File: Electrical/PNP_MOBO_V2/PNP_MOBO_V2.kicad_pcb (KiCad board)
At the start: 4 copper layers, 0 parts

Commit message: wip pcbv2
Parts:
- added A10: Pololu_Breakout_DRV8825, Module:Pololu_Breakout-16_15.2x20.3mm, F.Cu at (122.8, 87.6)
- added A5: Pololu_Breakout_DRV8825, Module:Pololu_Breakout-16_15.2x20.3mm, F.Cu at (70.7, 87.6)
- added A6: Pololu_Breakout_DRV8825, Module:Pololu_Breakout-16_15.2x20.3mm, F.Cu at (96.7, 61.6)
- added A7: Pololu_Breakout_DRV8825, Module:Pololu_Breakout-16_15.2x20.3mm, F.Cu at (96.7, 87.6)
- added A8: Pololu_Breakout_DRV8825, Module:Pololu_Breakout-16_15.2x20.3mm, F.Cu at (122.7, 61.6)
- added A9: Pololu_Breakout_DRV8825, Module:Pololu_Breakout-16_15.2x20.3mm, F.Cu at (70.8, 61.6)
- added C1: 0.1uf, Capacitor_SMD:C_0603_1608Metric_Pad1.08x0.95mm_HandSolder, F.Cu at (-17.8, 2.99)
- added C12: 10uf, Capacitor_SMD:C_0603_1608Metric_Pad1.08x0.95mm_HandSolder, F.Cu at (-13.5, 2.99)
- added C13: 0.1uf, Capacitor_SMD:C_0603_1608Metric_Pad1.08x0.95mm_HandSolder, F.Cu at (-13.5, 5.50)
- added C16: 10uf, Capacitor_SMD:C_0603_1608Metric_Pad1.08x0.95mm_HandSolder, F.Cu at (-13.5, 8.01)
- added C17: 0.1uf, Capacitor_SMD:C_0603_1608Metric_Pad1.08x0.95mm_HandSolder, F.Cu at (-13.5, 10.5)
- added C2: 10uf, Capacitor_SMD:C_0603_1608Metric_Pad1.08x0.95mm_HandSolder, F.Cu at (-17.8, 5.50)
- added C20: 100uF, Capacitor_SMD:CP_Elec_8x10, F.Cu at (160.0, 72.6)
- added C21: 0.1uF, Capacitor_SMD:C_0603_1608Metric_Pad1.08x0.95mm_HandSolder, F.Cu at (-13.5, 13.0)
- added C22: 0.1uF, Capacitor_SMD:C_0603_1608Metric_Pad1.08x0.95mm_HandSolder, F.Cu at (149.3, 110.5)
- added C23: 100uF, Capacitor_SMD:CP_Elec_8x10, F.Cu at (88.0, 94.3)
- added C24: 0.1uF, Capacitor_SMD:C_0603_1608Metric_Pad1.08x0.95mm_HandSolder, F.Cu at (149.3, 113.0)
- added C25: 100uF, Capacitor_SMD:CP_Elec_8x10, F.Cu at (114.6, 68.3)
- added C26: 0.1uF, Capacitor_SMD:C_0603_1608Metric_Pad1.08x0.95mm_HandSolder, F.Cu at (149.3, 115.5)
- added C27: 100uF, Capacitor_SMD:CP_Elec_8x10, F.Cu at (114.8, 94.3)
- added C28: 0.1uF, Capacitor_SMD:C_0603_1608Metric_Pad1.08x0.95mm_HandSolder, F.Cu at (149.3, 118.0)
- added C29: 100uF, Capacitor_SMD:CP_Elec_8x10, F.Cu at (140.6, 67.9)
- added C3: 100uF, Capacitor_SMD:CP_Elec_8x10, F.Cu at (76.2, 25.6)
- added C30: 0.1uF, Capacitor_SMD:C_0603_1608Metric_Pad1.08x0.95mm_HandSolder, F.Cu at (149.3, 120.5)
- added C31: 100uF, Capacitor_SMD:CP_Elec_8x10, F.Cu at (88.6, 68.3)
- added C32: 0.1uF, Capacitor_SMD:C_0603_1608Metric_Pad1.08x0.95mm_HandSolder, F.Cu at (149.3, 123.0)
- added C33: 100uF, Capacitor_SMD:CP_Elec_8x10, F.Cu at (140.8, 94.3)
- added C7: 1uf/16V 10%, Capacitor_SMD:C_0603_1608Metric_Pad1.08x0.95mm_HandSolder, F.Cu at (-17.8, 8.01)
- added C8: 0.1uf, Capacitor_SMD:C_0603_1608Metric_Pad1.08x0.95mm_HandSolder, F.Cu at (-17.8, 10.5)
- added C9: 0.1uf, Capacitor_SMD:C_0603_1608Metric_Pad1.08x0.95mm_HandSolder, F.Cu at (-17.8, 13.0)
- added D1: D_TVS, Diode_SMD:D_SMB, F.Cu at (151.6, 81.6)
- added D2: D, Diode_SMD:D_SMB, F.Cu at (180.8, 43.2)
- added D3: SP0503BAHT, Package_TO_SOT_SMD:SOT-143, F.Cu at (76.0, 34.8)
- added D5: LED, LED_SMD:LED_0603_1608Metric, F.Cu at (-44.4, 22.1)
- added D6: LED, LED_SMD:LED_0603_1608Metric, F.Cu at (-44.4, 24.7)
- added D7: NUP2105L, Package_TO_SOT_SMD:SOT-23, F.Cu at (159.1, 35.6)
- added D8: D, Diode_SMD:D_SMB, F.Cu at (180.8, 48.8)
- added D9: D, Diode_SMD:D_SMB, F.Cu at (180.8, 54.4)
- added H1: MountingHole, MountingHole:MountingHole_3.2mm_M3, F.Cu at (64.4, 25.0)
- added H2: MountingHole, MountingHole:MountingHole_3.2mm_M3, F.Cu at (64.4, 95.0)
- added H3: MountingHole, MountingHole:MountingHole_3.2mm_M3, F.Cu at (164.4, 95.0)
- added H4: MountingHole, MountingHole:MountingHole_3.2mm_M3, F.Cu at (164.4, 25.0)
- added J1: USB_C_Receptacle_USB2.0_16P, Connector_USB:USB_C_Receptacle_GCT_USB4105-xx-A_16P_TopMnt_Horizontal, F.Cu at (64.8, 34.9)
- added J10: Conn_01x04_Pin, Connector_JST:JST_XH_B4B-XH-A_1x04_P2.50mm_Vertical, F.Cu at (105.6, 68.3)
- added J11: Conn_01x04_Pin, Connector_JST:JST_XH_B4B-XH-A_1x04_P2.50mm_Vertical, F.Cu at (105.6, 94.3)
- added J12: Conn_01x04_Pin, Connector_JST:JST_XH_B4B-XH-A_1x04_P2.50mm_Vertical, F.Cu at (131.6, 68.4)
- added J13: Conn_01x04_Pin, Connector_JST:JST_XH_B4B-XH-A_1x04_P2.50mm_Vertical, F.Cu at (79.7, 68.3)
- added J14: Conn_01x04_Pin, Connector_JST:JST_XH_B4B-XH-A_1x04_P2.50mm_Vertical, F.Cu at (131.8, 94.3)
- added J15: Conn_01x04_Pin, Connector_PinSocket_2.54mm:PinSocket_1x04_P2.54mm_Vertical, F.Cu at (144.2, 22.4)
- added J16: Conn_01x04_Pin, Connector_PinSocket_2.54mm:PinSocket_1x04_P2.54mm_Vertical, F.Cu at (158.8, 22.4)
- added J17: Conn_01x02_Pin, Connector_Molex:Molex_KK-254_AE-6410-02A_1x02_P2.54mm_Vertical, F.Cu at (63.8, 82.8)
- added J18: Conn_01x02_Pin, Connector_Molex:Molex_KK-254_AE-6410-02A_1x02_P2.54mm_Vertical, F.Cu at (63.8, 72.8)
- added J19: Conn_01x02_Pin, Connector_Molex:Molex_KK-254_AE-6410-02A_1x02_P2.54mm_Vertical, F.Cu at (63.8, 63.2)
- added J3: Conn_01x02_Pin, Connector_Molex:Molex_KK-254_AE-6410-02A_1x02_P2.54mm_Vertical, F.Cu at (165.0, 63.5)
- added J4: Conn_01x03_Pin, Connector_PinHeader_2.54mm:PinHeader_1x03_P2.54mm_Vertical, F.Cu at (131.6, 24.5)
- added J5: Conn_01x02_Pin, Connector_Molex:Molex_KK-254_AE-6410-02A_1x02_P2.54mm_Vertical, F.Cu at (165.0, 55.7)
- added J6: Conn_01x03_Pin, Connector_Molex:Molex_KK-254_AE-6410-03A_1x03_P2.54mm_Vertical, F.Cu at (165.0, 39.3)
- added J7: Conn_01x02_Pin, Connector_Molex:Molex_KK-254_AE-6410-02A_1x02_P2.54mm_Vertical, F.Cu at (165.0, 48.1)
- added J8: Barrel_Jack_MountingPin, Connector_BarrelJack:BarrelJack_CUI_PJ-063AH_Horizontal, F.Cu at (156.8, 83.6)
- added J9: Conn_01x04_Pin, Connector_JST:JST_XH_B4B-XH-A_1x04_P2.50mm_Vertical, F.Cu at (79.6, 94.3)
- added Q1: IRLML6244, Package_TO_SOT_SMD:SOT-23, F.Cu at (187.4, 42.9)
- added Q2: IRLML6244, Package_TO_SOT_SMD:SOT-23, F.Cu at (187.4, 47.5)
- added Q4: IRLML6244, Package_TO_SOT_SMD:SOT-23, F.Cu at (187.4, 52.1)
- added R1: 10k 1%, Resistor_SMD:R_0603_1608Metric_Pad0.98x0.95mm_HandSolder, F.Cu at (-9.13, 2.99)
- added R10: 10k 1%, Resistor_SMD:R_0603_1608Metric_Pad0.98x0.95mm_HandSolder, F.Cu at (-4.78, 5.50)
- added R11: 10k, Resistor_SMD:R_0603_1608Metric_Pad0.98x0.95mm_HandSolder, F.Cu at (174.4, 49.3)
- added R12: 120, Resistor_SMD:R_0603_1608Metric_Pad0.98x0.95mm_HandSolder, F.Cu at (-4.78, 8.01)
- added R13: 10k, Resistor_SMD:R_0603_1608Metric_Pad0.98x0.95mm_HandSolder, F.Cu at (174.4, 51.8)
- added R14: 100, Resistor_SMD:R_0603_1608Metric_Pad0.98x0.95mm_HandSolder, F.Cu at (174.4, 54.3)
- added R15: 100, Resistor_SMD:R_0603_1608Metric_Pad0.98x0.95mm_HandSolder, F.Cu at (174.4, 56.8)
- added R16: 10k, Resistor_SMD:R_0603_1608Metric_Pad0.98x0.95mm_HandSolder, F.Cu at (174.4, 59.3)
- added R17: 100, Resistor_SMD:R_0603_1608Metric_Pad0.98x0.95mm_HandSolder, F.Cu at (174.4, 61.8)
- added R2: 22, Resistor_SMD:R_0603_1608Metric_Pad0.98x0.95mm_HandSolder, F.Cu at (-9.13, 5.50)
- added R3: 22, Resistor_SMD:R_0603_1608Metric_Pad0.98x0.95mm_HandSolder, F.Cu at (-9.13, 8.01)
- added R36: 330, Resistor_SMD:R_0603_1608Metric_Pad0.98x0.95mm_HandSolder, F.Cu at (-4.78, 10.5)
- added R37: 330, Resistor_SMD:R_0603_1608Metric_Pad0.98x0.95mm_HandSolder, F.Cu at (-4.78, 13.0)
- added R4: 10k, Resistor_SMD:R_0603_1608Metric_Pad0.98x0.95mm_HandSolder, F.Cu at (43.9, 57.6)
- added R40: 10k 1%, Resistor_SMD:R_0603_1608Metric_Pad0.98x0.95mm_HandSolder, F.Cu at (89.7, 109.0)
- added R41: 10k 1%, Resistor_SMD:R_0603_1608Metric_Pad0.98x0.95mm_HandSolder, F.Cu at (95.2, 107.3)
- added R42: 10k 1%, Resistor_SMD:R_0603_1608Metric_Pad0.98x0.95mm_HandSolder, F.Cu at (95.2, 109.8)
- added R43: 10k 1%, Resistor_SMD:R_0603_1608Metric_Pad0.98x0.95mm_HandSolder, F.Cu at (95.2, 112.4)
- added R44: 10k 1%, Resistor_SMD:R_0603_1608Metric_Pad0.98x0.95mm_HandSolder, F.Cu at (95.2, 114.9)
- added R45: 10k 1%, Resistor_SMD:R_0603_1608Metric_Pad0.98x0.95mm_HandSolder, F.Cu at (95.2, 117.4)
- added R46: 10k 1%, Resistor_SMD:R_0603_1608Metric_Pad0.98x0.95mm_HandSolder, F.Cu at (95.2, 119.9)
- added R47: 10k 1%, Resistor_SMD:R_0603_1608Metric_Pad0.98x0.95mm_HandSolder, F.Cu at (95.2, 122.4)
- added R48: 0, Resistor_SMD:R_0402_1005Metric, F.Cu at (104.7, 107.0)
- added R49: 0, Resistor_SMD:R_0402_1005Metric, F.Cu at (104.7, 109.0)
- added R5: 5.1k, Resistor_SMD:R_0603_1608Metric_Pad0.98x0.95mm_HandSolder, F.Cu at (-9.13, 10.5)
- added R50: 0, Resistor_SMD:R_0402_1005Metric, F.Cu at (104.7, 111.0)
- added R51: 0, Resistor_SMD:R_0402_1005Metric, F.Cu at (104.7, 113.0)
- added R52: 0, Resistor_SMD:R_0402_1005Metric, F.Cu at (104.7, 115.0)
- added R53: 0, Resistor_SMD:R_0402_1005Metric, F.Cu at (104.7, 117.0)
- added R54: 0, Resistor_SMD:R_0402_1005Metric, F.Cu at (104.7, 118.9)
- added R55: 0, Resistor_SMD:R_0402_1005Metric, F.Cu at (107.6, 107.0)
- added R56: 0, Resistor_SMD:R_0402_1005Metric, F.Cu at (107.6, 109.0)
- added R57: 0, Resistor_SMD:R_0402_1005Metric, F.Cu at (107.6, 111.0)
- added R58: 0, Resistor_SMD:R_0402_1005Metric, F.Cu at (107.6, 113.0)
- added R59: 0, Resistor_SMD:R_0402_1005Metric, F.Cu at (107.6, 115.0)
- added R6: 5.1k, Resistor_SMD:R_0603_1608Metric_Pad0.98x0.95mm_HandSolder, F.Cu at (-9.13, 13.0)
- added R60: 10k 1%, Resistor_SMD:R_0603_1608Metric_Pad0.98x0.95mm_HandSolder, F.Cu at (128.3, 102.1)
- added R61: 10k 1%, Resistor_SMD:R_0603_1608Metric_Pad0.98x0.95mm_HandSolder, F.Cu at (128.3, 104.6)
- added R62: 0, Resistor_SMD:R_0402_1005Metric, F.Cu at (107.6, 117.0)
- added R63: 0, Resistor_SMD:R_0402_1005Metric, F.Cu at (107.6, 118.9)
- added R64: 0, Resistor_SMD:R_0402_1005Metric, F.Cu at (110.5, 107.0)
- added R65: 10k 1%, Resistor_SMD:R_0603_1608Metric_Pad0.98x0.95mm_HandSolder, F.Cu at (128.3, 107.1)
- added R66: 10k 1%, Resistor_SMD:R_0603_1608Metric_Pad0.98x0.95mm_HandSolder, F.Cu at (128.3, 109.6)
- added R67: 0, Resistor_SMD:R_0402_1005Metric, F.Cu at (110.5, 109.0)
- added R68: 0, Resistor_SMD:R_0402_1005Metric, F.Cu at (110.5, 111.0)
- added R69: 0, Resistor_SMD:R_0402_1005Metric, F.Cu at (110.5, 113.0)
- added R7: 1, Resistor_SMD:R_0603_1608Metric_Pad0.98x0.95mm_HandSolder, F.Cu at (-4.78, 2.99)
- added R8: 10k, Resistor_SMD:R_0603_1608Metric_Pad0.98x0.95mm_HandSolder, F.Cu at (47.7, 61.0)
- added R9: 10k, Resistor_SMD:R_0603_1608Metric_Pad0.98x0.95mm_HandSolder, F.Cu at (44.9, 65.3)
- added SW1: SW_Push, Button_Switch_SMD:SW_SPST_PTS647_Sx38, F.Cu at (-2.15, -21.1)
- added SW2: SW_Push, Button_Switch_SMD:SW_SPST_PTS647_Sx38, F.Cu at (-2.15, -14.6)
- added TP1: TestPoint, TestPoint:TestPoint_Pad_D2.0mm, F.Cu at (-4.30, -38.5)
- added TP2: TestPoint, TestPoint:TestPoint_Pad_D2.0mm, F.Cu at (-4.30, -34.4)
- added TP4: TestPoint, TestPoint:TestPoint_Pad_D2.0mm, F.Cu at (-4.30, -30.4)
- added TP5: TestPoint, TestPoint:TestPoint_Pad_D2.0mm, F.Cu at (-4.30, -26.3)
- added TP6: TestPoint, TestPoint:TestPoint_Pad_D2.0mm, F.Cu at (-0.25, -38.5)
- added TP7: TestPoint, TestPoint:TestPoint_Pad_D2.0mm, F.Cu at (-0.25, -34.4)
- added TP8: TestPoint, TestPoint:TestPoint_Pad_D2.0mm, F.Cu at (-0.25, -30.4)
- added U1: ESP32-S3-WROOM-1, RF_Module:ESP32-S3-WROOM-1, F.Cu at (119.2, 26.7)
- added U3: SN65HVD230, Package_SO:SOIC-8_3.9x4.9mm_P1.27mm, F.Cu at (151.3, 35.7)
- added U4: AMS1117-3.3, Package_TO_SOT_SMD:SOT-223-3_TabPin2, F.Cu at (87.8, 25.2)
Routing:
- added copper zone on In2.Cu, net 12V
- added copper zone on F.Cu, net 3V3
- added copper zone on In1.Cu, net GND
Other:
- board outline added: 110 x 80 mm

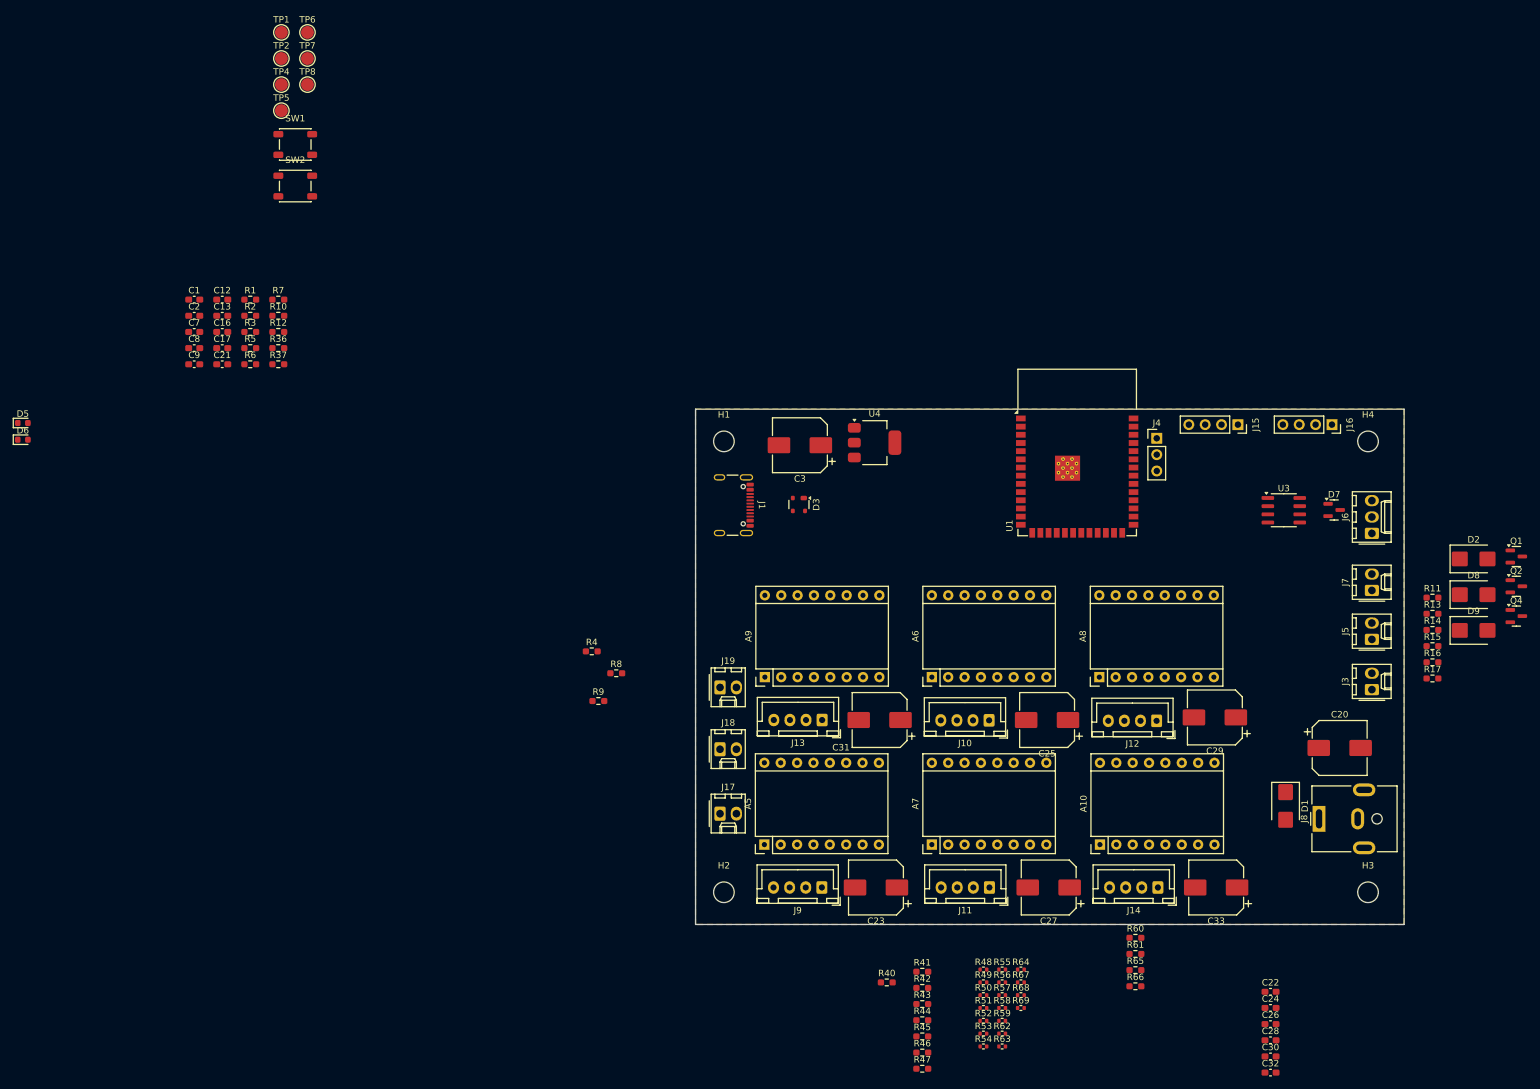
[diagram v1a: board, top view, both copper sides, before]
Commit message: rooting done, only last check and test missing
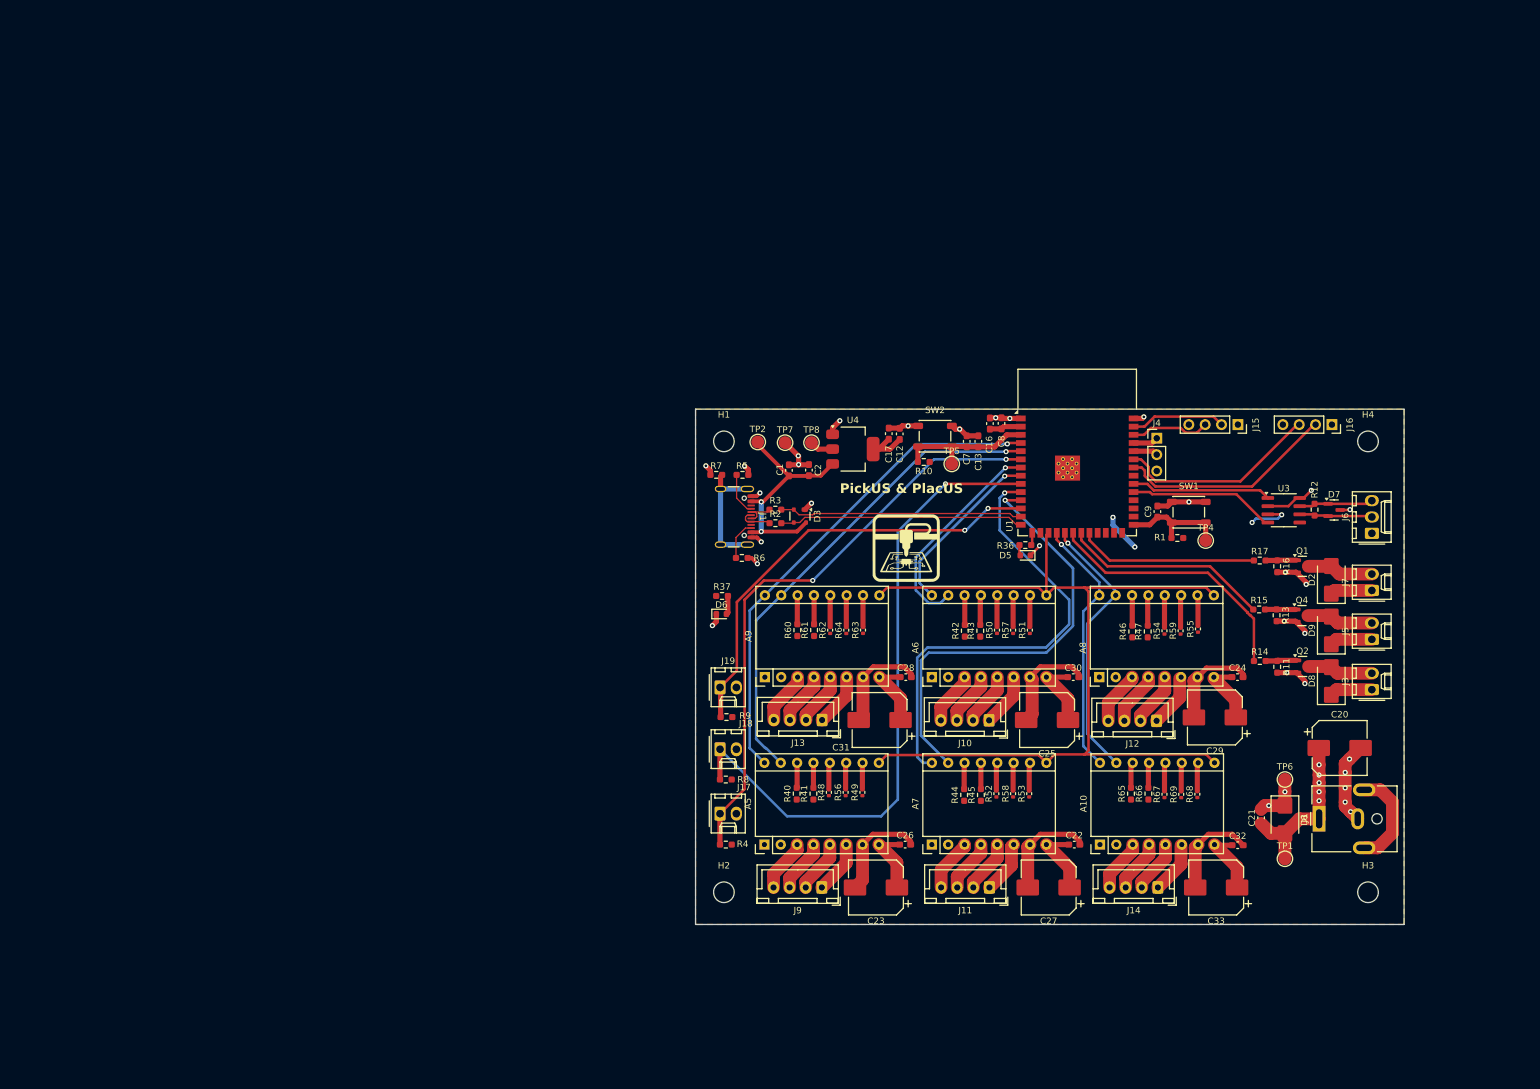
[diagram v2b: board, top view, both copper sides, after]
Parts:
- removed C3: 100uF, Capacitor_SMD:CP_Elec_8x10
- added G***: LOGO, LOGO, F.Cu at (92.9, 41.7)
- moved TP1 201.8 mm to (151.5, 89.8)
- moved TP6 191.0 mm to (151.5, 77.5)
- moved C21 176.0 mm to (147.8, 83.4), turned to 90 degrees
- moved R12 163.2 mm to (156.1, 35.6), turned to 90 degrees
- moved TP4 160.0 mm to (139.2, 40.4)
- moved D5 157.0 mm to (111.2, 42.7), turned to 180 degrees
- moved C9 151.3 mm to (131.7, 35.9), turned to 90 degrees
- moved SW1 150.0 mm to (136.6, 36.0)
- moved R1 148.6 mm to (134.8, 40.0)
- moved C8 125.9 mm to (107.5, 22.2), turned to -90 degrees
- moved C7 121.1 mm to (102.1, 25.0), turned to 90 degrees
- moved C16 120.0 mm to (105.7, 22.2), turned to -90 degrees
- moved R36 119.9 mm to (111.2, 41.1), turned to 180 degrees
- moved C13 119.0 mm to (103.9, 25.0), turned to 90 degrees
- moved TP5 117.6 mm to (99.8, 28.5)
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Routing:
- net GND: track 0.00 -> 189.4 mm, vias 0 -> 32
- net DRIVE_EN: track 0.00 -> 144.3 mm
- net 12V: track 0.00 -> 111.7 mm, vias 0 -> 5
- net LIM_Y: track 0.00 -> 101.5 mm, vias 0 -> 1
- net LIM_X: track 0.00 -> 91.5 mm, vias 0 -> 2
- net DRIVE_X_DIR: track 0.00 -> 77.5 mm, vias 0 -> 1
- net DRIVE_X_STP: track 0.00 -> 75.7 mm, vias 0 -> 1
- net DRIVE_Z_DIR: track 0.00 -> 71.6 mm, vias 0 -> 1
- net DRIVE_Z_STP: track 0.00 -> 69.8 mm, vias 0 -> 1
- net LIM_Z: track 0.00 -> 69.1 mm, vias 0 -> 2
- net DRIVE_YAW_STP: track 0.00 -> 42.7 mm, vias 0 -> 1
- net SW_PUMP: track 0.00 -> 40.9 mm
- net DRIVE_YAW_DIR: track 0.00 -> 40.5 mm, vias 0 -> 1
- net /D-: track 0.00 -> 38.2 mm
- net /D+: track 0.00 -> 38.0 mm
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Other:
- board text added: "PickUS & PlacUS"

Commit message: add i bom and fabrication file
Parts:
- added REF1: Conn_01x01_Pin, Connector_PinHeader_1.00mm:PinHeader_1x01_P1.00mm_Vertical, F.Cu at (64.4, 95.0)
- added REF2: Conn_01x01_Pin, Connector_PinHeader_1.00mm:PinHeader_1x01_P1.00mm_Vertical, F.Cu at (153.8, 95.6)
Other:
- board text added: "12V"
- board text added: "CHIP_PU"
- board text added: "DRIVE X"
- board text added: "DRIVE Y"
- board text added: "DRIVE YAW"
- board text added: "DRIVE Z"
- board text added: "GND"
- board text added: "GPIO0"
- board text added: "H L G"
- board text added: "LIM X"
- board text added: "LIM Y"
- board text added: "LIM Z"
- board text added: "P1 G C D V"
- board text added: "P2 G C D V"
- board text added: "PUMP"
- board text added: "VALVE 1"
- board text added: "VAVLE 2"
- board text added: "VBUS GND 3V3"

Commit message: fix: last change before order
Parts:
- turned C20 to 180 degrees
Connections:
- J8 pad 1: 12V -> GND
- J8 pad 2: GND -> 12V
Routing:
- net 12V: track 111.7 -> 121.3 mm, vias 5 -> 7
- net GND: track 189.4 -> 187.7 mm, vias 32 -> 30
